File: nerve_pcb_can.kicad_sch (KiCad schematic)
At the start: 6 parts, among them J8 CAN1, J9 CAN2, U6 TJA1051T/3, U7 TJA1051T/3

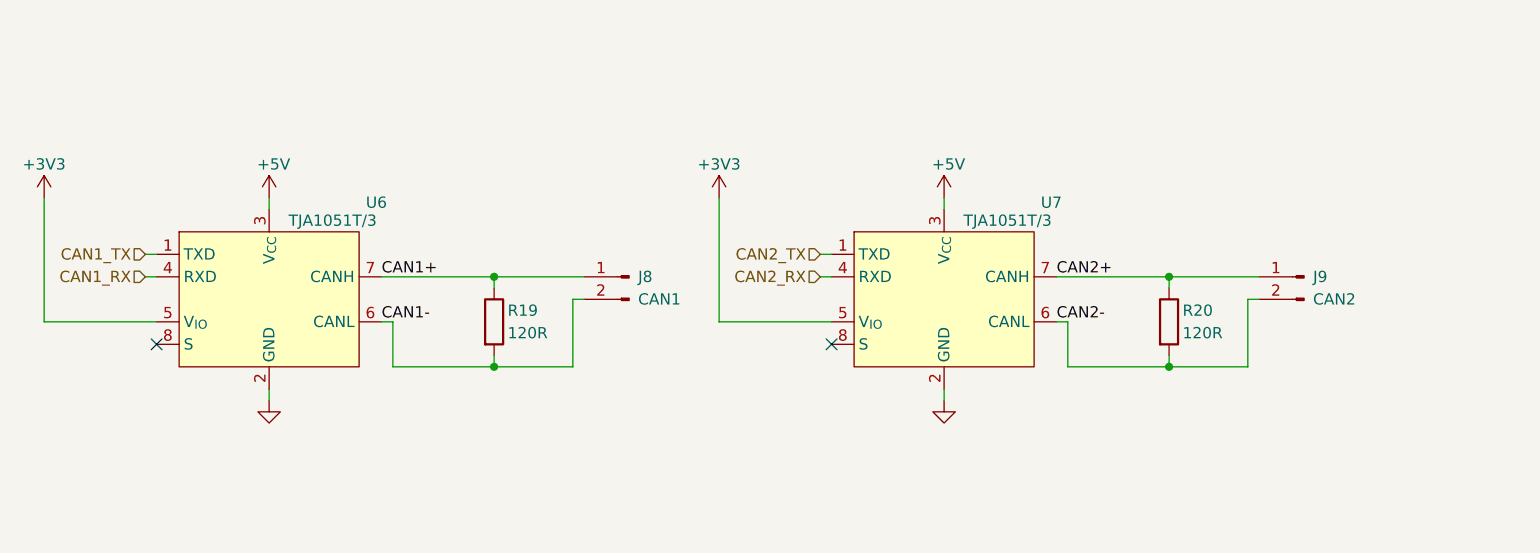
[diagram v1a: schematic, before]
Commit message: Switch to split CAN termination
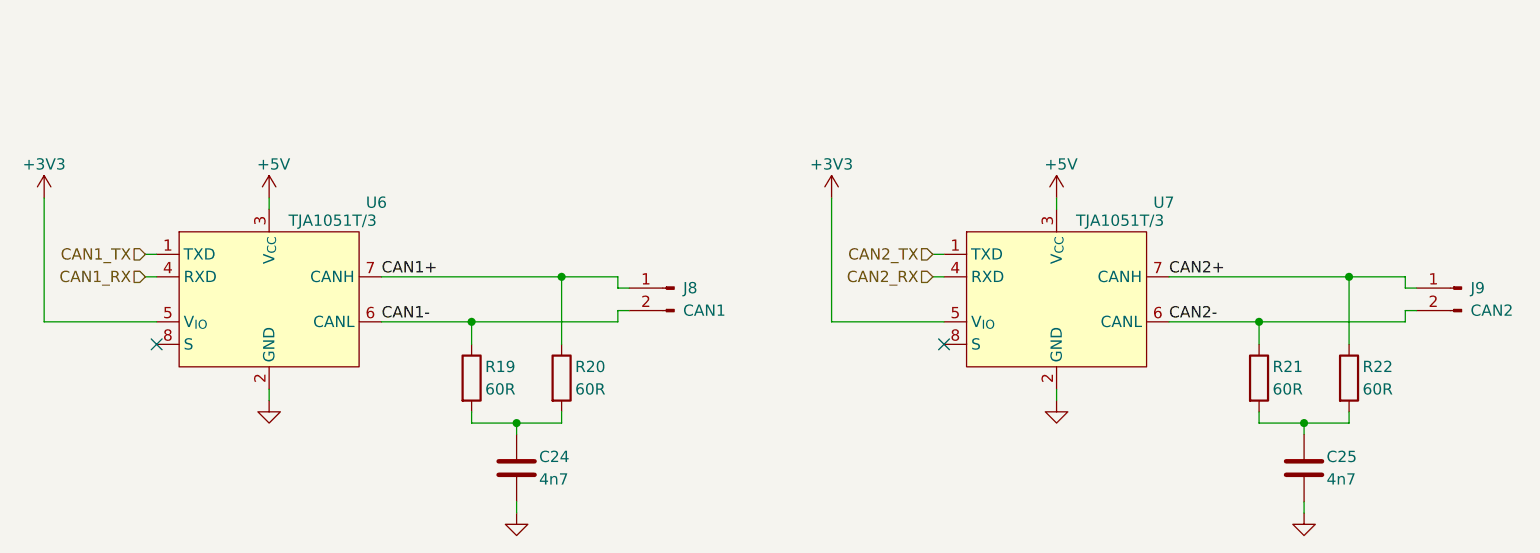
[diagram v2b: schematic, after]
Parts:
- added C24, C25: 4n7, Capacitor_SMD:C_0603_1608Metric, symbol Device:C
- added R21, R22: 60R, Resistor_SMD:R_0603_1608Metric, symbol Device:R
- R19, R20: value 120R -> 60R
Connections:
- net CAN1+: now also R20.1; no longer R19.1
- net CAN1-: now also R19.1; no longer R19.2
- net CAN2+: now also R22.1; no longer R20.1
- net CAN2-: now also R21.1; no longer R20.2
- net GND: now also C24.2, C25.2
- new net: C25.1, R21.2, R22.2
- new net: C24.1, R19.2, R20.2
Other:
- moved on the sheet: J8, U7

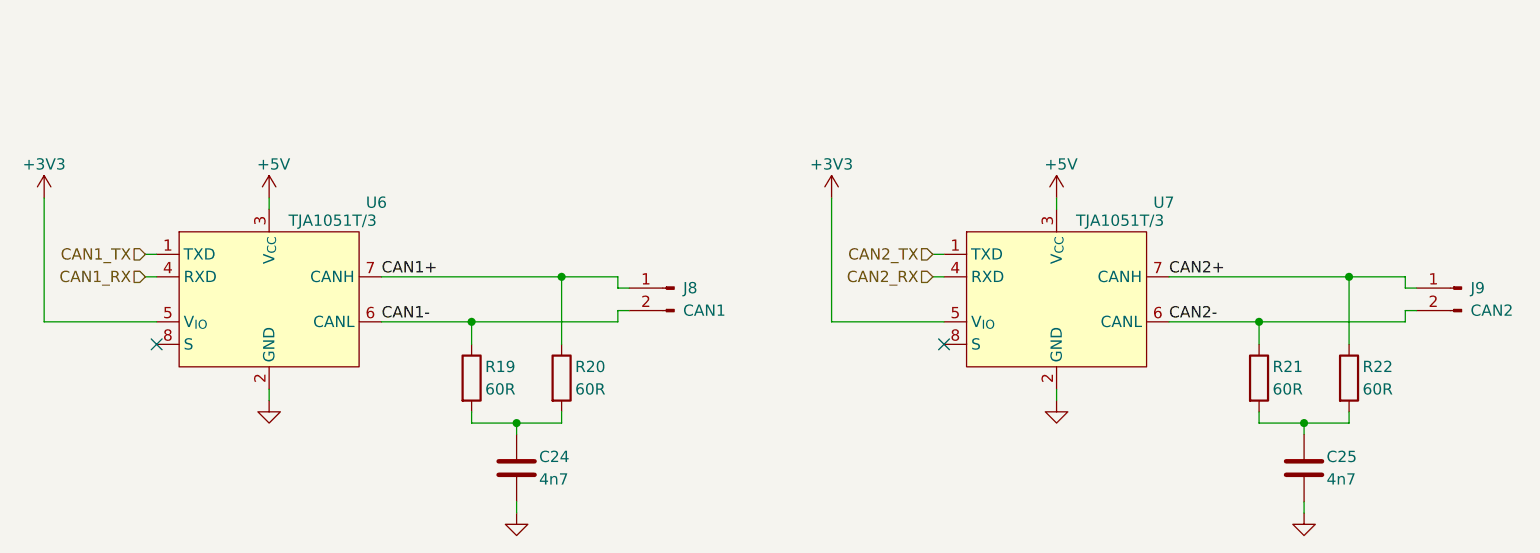
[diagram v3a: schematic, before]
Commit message: Add minor decoupling caps
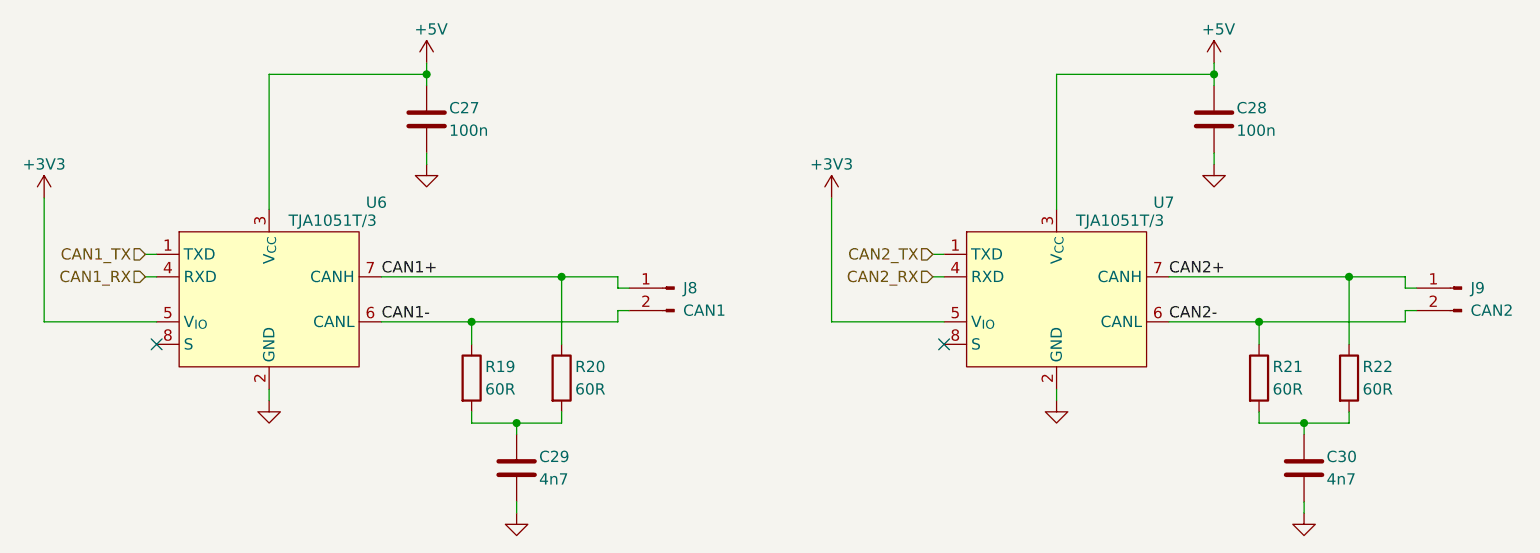
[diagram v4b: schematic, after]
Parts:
- added C27, C28: 100n, Capacitor_SMD:C_0603_1608Metric, symbol Device:C
- renumbered C24 to C29, C25 to C30
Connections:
- net +5V: now also C27.1, C28.1
- net GND: now also C27.2, C28.2

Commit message: Add WS2812B decoupling caps and PCB cleanup
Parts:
- renumbered C27 to C29, C28 to C30, C29 to C31, C30 to C32
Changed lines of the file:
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@@
 		(dnp no)
 		(fields_autoplaced yes)
-		(property "Reference" "#PWR090"
+		(property "Reference" "#PWR092"
 			(at 111.76 127 0)
 			(effects
@@
 			(project "nerve_pcb"
 				(path "/c0277862-b3f2-4e0e-986f-34702f0543f0/4fcd2c12-d66e-4aef-b6ae-64082d99e104"
-					(reference "#PWR090")
+					(reference "#PWR092")
 					(unit 1)
 				)
@@
 		(dnp no)
 		(fields_autoplaced yes)
-		(property "Reference" "#PWR086"
+		(property "Reference" "#PWR088"
 			(at 129.54 100.33 0)
 			(effects
@@
 			(project "nerve_pcb"
 				(path "/c0277862-b3f2-4e0e-986f-34702f0543f0/4fcd2c12-d66e-4aef-b6ae-64082d99e104"
-					(reference "#PWR086")
+					(reference "#PWR088")
 					(unit 1)
 				)
@@
 		(on_board yes)
 		(dnp no)
-		(property "Reference" "#PWR088"
+		(property "Reference" "#PWR090"
 			(at 86.36 101.6 0)
 			(effects
@@
 			(project "nerve_pcb"
 				(path "/c0277862-b3f2-4e0e-986f-34702f0543f0/4fcd2c12-d66e-4aef-b6ae-64082d99e104"
-					(reference "#PWR088")
+					(reference "#PWR090")
 					(unit 1)
 				)
@@
 		(on_board yes)
 		(dnp no)
-		(property "Reference" "#PWR084"
+		(property "Reference" "#PWR086"
 			(at 129.54 86.36 0)
 			(effects
@@
 			(project "nerve_pcb"
 				(path "/c0277862-b3f2-4e0e-986f-34702f0543f0/4fcd2c12-d66e-4aef-b6ae-64082d99e104"
-					(reference "#PWR084")
+					(reference "#PWR086")
 					(unit 1)
 				)
@@
 		(on_board yes)
 		(dnp no)
-		(property "Reference" "#PWR089"
+		(property "Reference" "#PWR091"
 			(at 175.26 101.6 0)
 			(effects
@@
 			(project "nerve_pcb"
 				(path "/c0277862-b3f2-4e0e-986f-34702f0543f0/4fcd2c12-d66e-4aef-b6ae-64082d99e104"
-					(reference "#PWR089")
+					(reference "#PWR091")
 					(unit 1)
 				)
@@
 		(on_board yes)
 		(dnp no)
-		(property "Reference" "C29"
+		(property "Reference" "C31"
 			(at 142.24 127 0)
 			(effects
@@
 			(project "nerve_pcb"
 				(path "/c0277862-b3f2-4e0e-986f-34702f0543f0/4fcd2c12-d66e-4aef-b6ae-64082d99e104"
-					(reference "C29")
+					(reference "C31")
 					(unit 1)
 				)
@@
 		(on_board yes)
 		(dnp no)
-		(property "Reference" "C27"
+		(property "Reference" "C29"
 			(at 132.08 87.63 0)
 			(effects
@@
 			(project "nerve_pcb"
 				(path "/c0277862-b3f2-4e0e-986f-34702f0543f0/4fcd2c12-d66e-4aef-b6ae-64082d99e104"
-					(reference "C27")
+					(reference "C29")
 					(unit 1)
 				)
@@
 		(dnp no)
 		(fields_autoplaced yes)
-		(property "Reference" "#PWR092"
+		(property "Reference" "#PWR094"
 			(at 139.7 139.7 0)
 			(effects
@@
 			(project "nerve_pcb"
 				(path "/c0277862-b3f2-4e0e-986f-34702f0543f0/4fcd2c12-d66e-4aef-b6ae-64082d99e104"
-					(reference "#PWR092")
+					(reference "#PWR094")
 					(unit 1)
 				)
@@
 		(on_board yes)
 		(dnp no)
-		(property "Reference" "C30"
+		(property "Reference" "C32"
 			(at 231.14 127 0)
 			(effects
@@
 			(project "nerve_pcb"
 				(path "/c0277862-b3f2-4e0e-986f-34702f0543f0/4fcd2c12-d66e-4aef-b6ae-64082d99e104"
-					(reference "C30")
+					(reference "C32")
 					(unit 1)
 				)
@@
 		(dnp no)
 		(fields_autoplaced yes)
-		(property "Reference" "#PWR093"
+		(property "Reference" "#PWR095"
 			(at 228.6 139.7 0)
 			(effects
@@
 			(project "nerve_pcb"
 				(path "/c0277862-b3f2-4e0e-986f-34702f0543f0/4fcd2c12-d66e-4aef-b6ae-64082d99e104"
-					(reference "#PWR093")
+					(reference "#PWR095")
 					(unit 1)
 				)
@@
 		(dnp no)
 		(fields_autoplaced yes)
-		(property "Reference" "#PWR087"
+		(property "Reference" "#PWR089"
 			(at 218.44 100.33 0)
 			(effects
@@
 			(project "nerve_pcb"
 				(path "/c0277862-b3f2-4e0e-986f-34702f0543f0/4fcd2c12-d66e-4aef-b6ae-64082d99e104"
-					(reference "#PWR087")
+					(reference "#PWR089")
 					(unit 1)
 				)
@@
 		(on_board yes)
 		(dnp no)
-		(property "Reference" "C28"
+		(property "Reference" "C30"
 			(at 220.98 87.63 0)
 			(effects
@@
 			(project "nerve_pcb"
 				(path "/c0277862-b3f2-4e0e-986f-34702f0543f0/4fcd2c12-d66e-4aef-b6ae-64082d99e104"
-					(reference "C28")
+					(reference "C30")
 					(unit 1)
 				)
@@
 		(dnp no)
 		(fields_autoplaced yes)
-		(property "Reference" "#PWR091"
+		(property "Reference" "#PWR093"
 			(at 200.66 127 0)
 			(effects
@@
 			(project "nerve_pcb"
 				(path "/c0277862-b3f2-4e0e-986f-34702f0543f0/4fcd2c12-d66e-4aef-b6ae-64082d99e104"
-					(reference "#PWR091")
+					(reference "#PWR093")
 					(unit 1)
 				)
@@
 		(on_board yes)
 		(dnp no)
-		(property "Reference" "#PWR085"
+		(property "Reference" "#PWR087"
 			(at 218.44 86.36 0)
 			(effects
@@
 			(project "nerve_pcb"
 				(path "/c0277862-b3f2-4e0e-986f-34702f0543f0/4fcd2c12-d66e-4aef-b6ae-64082d99e104"
-					(reference "#PWR085")
-					(unit 1)
-				)
+					(reference "#PWR087")
+					(unit 1)
+				)
